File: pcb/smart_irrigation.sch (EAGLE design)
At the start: 17 parts, among them IC1 7805DT, IC2 7833DT, J1 1X2-3.5MM

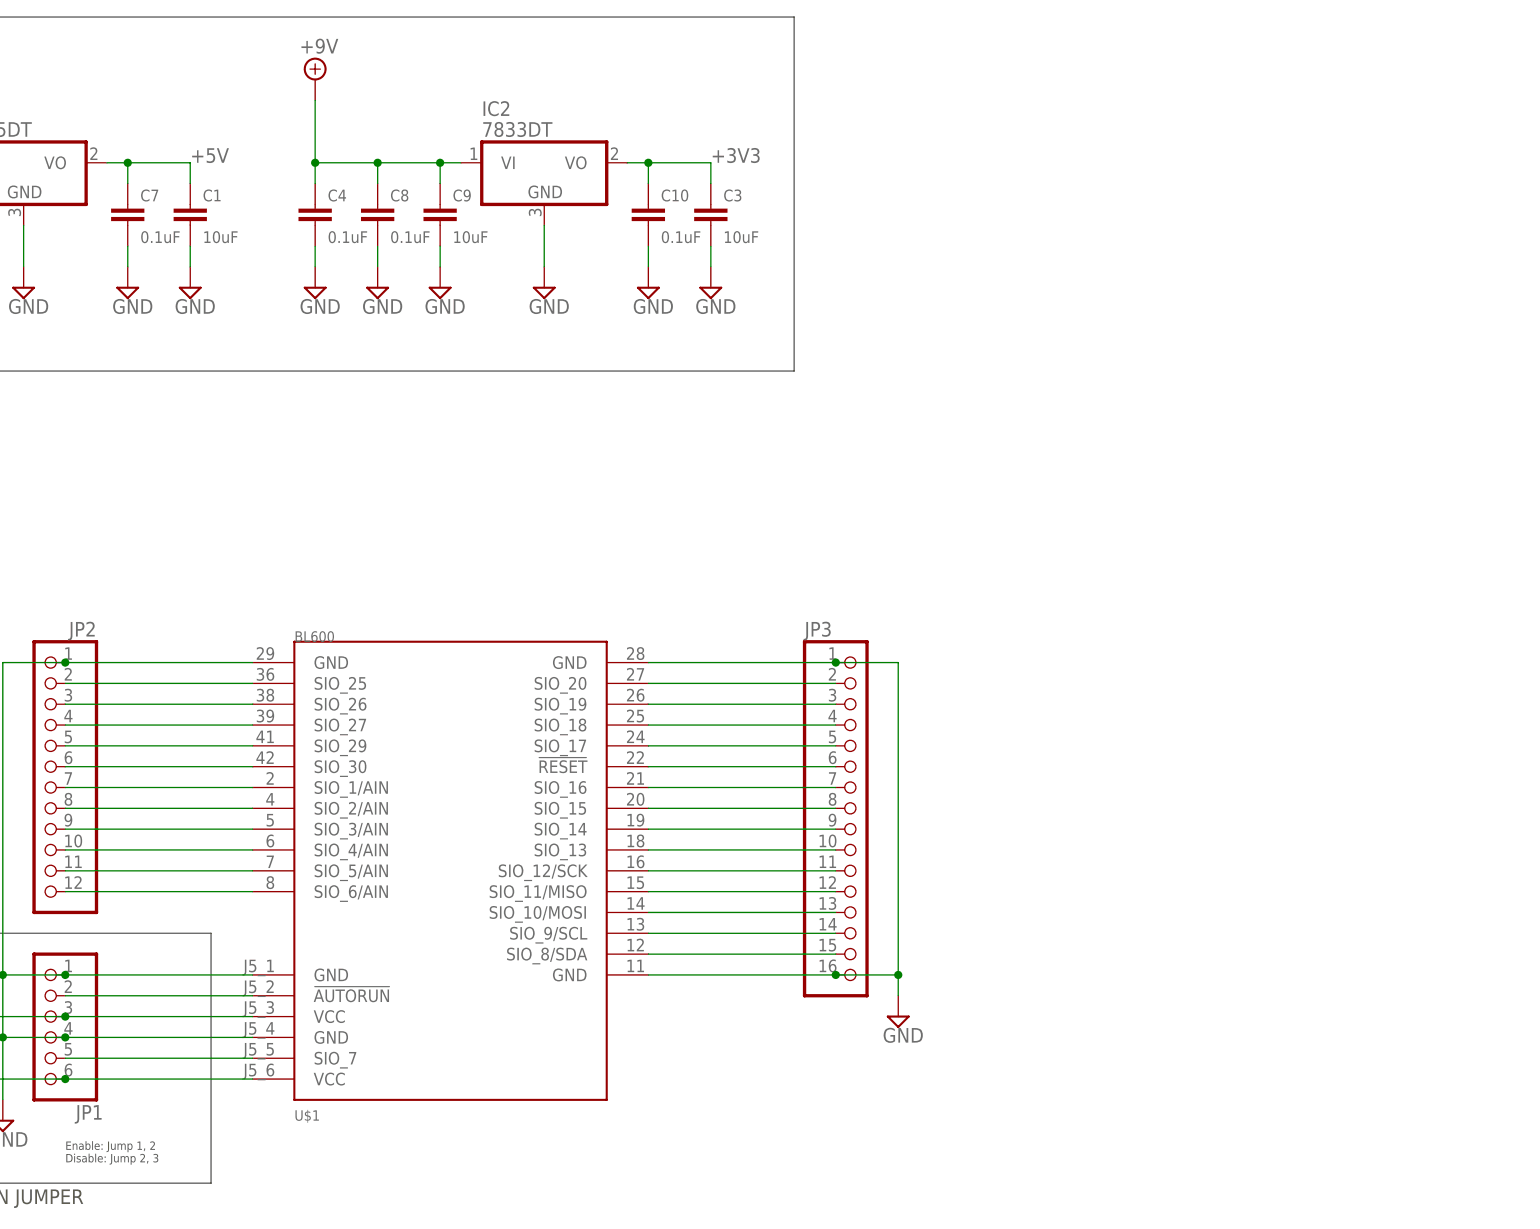
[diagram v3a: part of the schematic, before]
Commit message: PCB: Add RTC
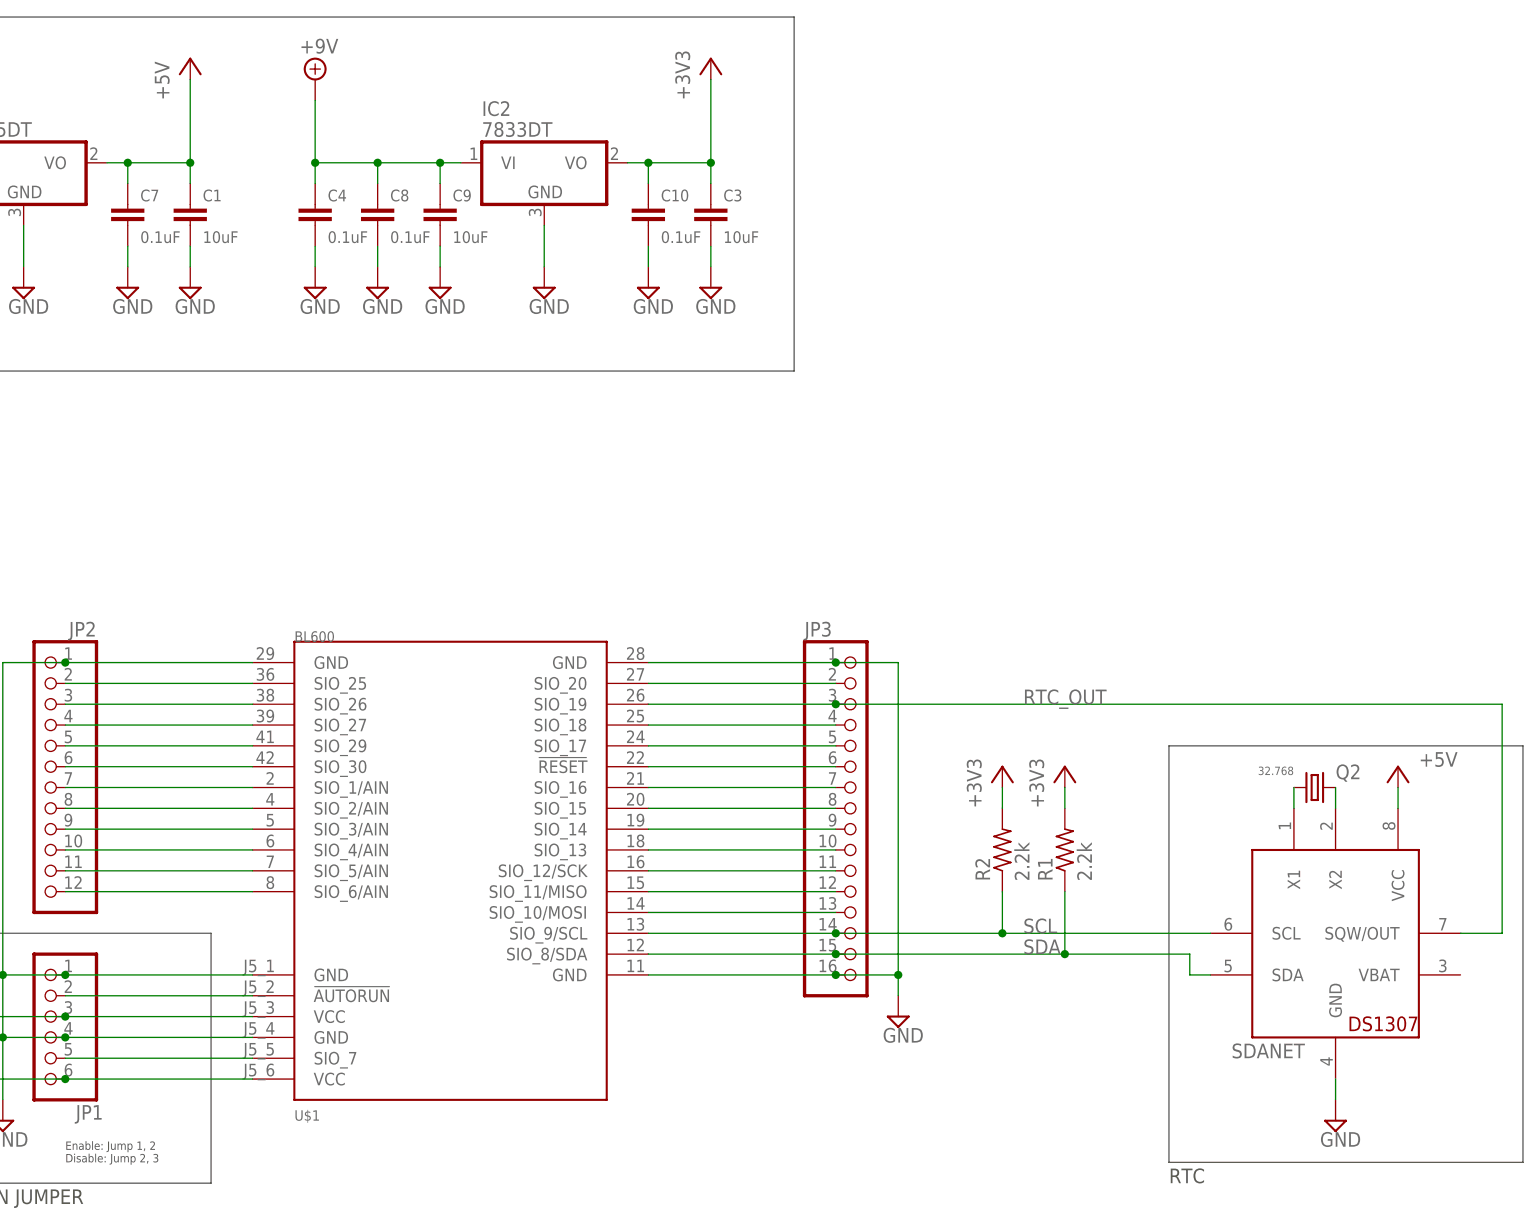
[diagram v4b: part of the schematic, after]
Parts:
- added Q2: 32.768, crystal:CRYSTALTC38H
- added R1, R2: 2.2k, rcl:R-US_M0805
- added SDANET: DS1307, adafruit:DS1307
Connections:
- removed net N$17: JP3.3, U$1.SIO_19
- removed net N$28: JP3.14, U$1.SIO_9/SCL
- removed net N$29: JP3.15, U$1.SIO_8/SDA
- new net N$15: Q2.2, SDANET.X2
- new net N$3: Q2.1, SDANET.X1
- new net RTC_OUT: JP3.3, SDANET.SQW/OUT, U$1.SIO_19
- new net SCL: JP3.14, R2.1, SDANET.SCL, U$1.SIO_9/SCL
- new net SDA: JP3.15, R1.1, SDANET.SDA, U$1.SIO_8/SDA
- net +3V3: now also R1.2, R2.2
- net +5V: now also SDANET.VCC
- net GND: now also SDANET.GND
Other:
- note added: "RTC"
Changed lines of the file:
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@@
 <part name="JP3" library="pinhead" deviceset="PINHD-1X16" device=""/>
 <part name="SUPPLY20" library="supply2" deviceset="GND" device=""/>
+<part name="SDANET" library="adafruit" deviceset="DS1307" device=""/>
+<part name="P+1" library="supply1" deviceset="+5V" device=""/>
+<part name="+3V2" library="supply1" deviceset="+3V3" device=""/>
+<part name="P+2" library="supply1" deviceset="+5V" device=""/>
+<part name="SUPPLY17" library="supply2" deviceset="GND" device=""/>
+<part name="Q2" library="crystal" deviceset="CRYSTAL" device="TC38H" value="32.768"/>
+<part name="R1" library="rcl" deviceset="R-US_" device="M0805" value="2.2k"/>
+<part name="R2" library="rcl" deviceset="R-US_" device="M0805" value="2.2k"/>
+<part name="+3V3" library="supply1" deviceset="+3V3" device=""/>
+<part name="+3V4" library="supply1" deviceset="+3V3" device=""/>
 </parts>
 <sheets>
@@
 <wire x1="58.42" y1="68.58" x2="58.42" y2="99.06" width="0.1524" layer="97"/>
 <text x="58.42" y="66.04" size="1.778" layer="97" font="vector">AUTORUN JUMPER</text>
+<wire x1="210.82" y1="71.12" x2="254" y2="71.12" width="0.1524" layer="97"/>
+<wire x1="254" y1="71.12" x2="254" y2="121.92" width="0.1524" layer="97"/>
+<wire x1="254" y1="121.92" x2="210.82" y2="121.92" width="0.1524" layer="97"/>
+<wire x1="210.82" y1="121.92" x2="210.82" y2="71.12" width="0.1524" layer="97"/>
+<text x="210.82" y="68.58" size="1.778" layer="97">RTC</text>
 </plain>
 <instances>
@@
 <instance part="JP3" gate="A" x="172.72" y="114.3"/>
 <instance part="SUPPLY20" gate="GND" x="177.8" y="88.9"/>
+<instance part="SDANET" gate="G$1" x="231.14" y="96.52"/>
+<instance part="P+1" gate="1" x="91.44" y="205.74"/>
+<instance part="+3V2" gate="G$1" x="154.94" y="205.74"/>
+<instance part="P+2" gate="1" x="238.76" y="119.38" smashed="yes">
+<attribute name="VALUE" x="241.3" y="119.38" size="1.778" layer="96"/>
+</instance>
+<instance part="SUPPLY17" gate="GND" x="231.14" y="76.2"/>
+<instance part="Q2" gate="G$1" x="228.6" y="116.84" smashed="yes">
+<attribute name="NAME" x="231.14" y="117.856" size="1.778" layer="95"/>
+<attribute name="VALUE" x="226.06" y="119.38" size="1.016" layer="96" rot="R180"/>
+</instance>
+<instance part="R1" gate="G$1" x="198.12" y="109.22" rot="R90"/>
+<instance part="R2" gate="G$1" x="190.5" y="109.22" rot="R90"/>
+<instance part="+3V3" gate="G$1" x="190.5" y="119.38"/>
+<instance part="+3V4" gate="G$1" x="198.12" y="119.38"/>
 </instances>
 <busses>
@@
 <junction x="177.8" y="93.98"/>
 </segment>
+<segment>
+<pinref part="SUPPLY17" gate="GND" pin="GND"/>
+<pinref part="SDANET" gate="G$1" pin="GND"/>
+<wire x1="231.14" y1="78.74" x2="231.14" y2="81.28" width="0.1524" layer="91"/>
+</segment>
 </net>
 <net name="+5V" class="0">
@@
 <pinref part="IC1" gate="A1" pin="VO"/>
 <wire x1="91.44" y1="193.04" x2="83.82" y2="193.04" width="0.1524" layer="91"/>
-<label x="91.44" y="193.04" size="1.778" layer="95"/>
 <pinref part="C1" gate="G$1" pin="1"/>
 <wire x1="83.82" y1="193.04" x2="81.28" y2="193.04" width="0.1524" layer="91"/>
@@
 <wire x1="83.82" y1="193.04" x2="83.82" y2="190.5" width="0.1524" layer="91"/>
 <junction x="83.82" y="193.04"/>
+<pinref part="P+1" gate="1" pin="+5V"/>
+<wire x1="91.44" y1="193.04" x2="91.44" y2="203.2" width="0.1524" layer="91"/>
+<junction x="91.44" y="193.04"/>
+</segment>
+<segment>
+<pinref part="SDANET" gate="G$1" pin="VCC"/>
+<pinref part="P+2" gate="1" pin="+5V"/>
+<wire x1="238.76" y1="116.84" x2="238.76" y2="114.3" width="0.1524" layer="91"/>
 </segment>
 </net>
@@
 <pinref part="IC2" gate="A1" pin="VO"/>
 <wire x1="154.94" y1="193.04" x2="147.32" y2="193.04" width="0.1524" layer="91"/>
-<label x="154.94" y="193.04" size="1.778" layer="95"/>
 <pinref part="C3" gate="G$1" pin="1"/>
 <wire x1="147.32" y1="193.04" x2="144.78" y2="193.04" width="0.1524" layer="91"/>
@@
 <wire x1="147.32" y1="193.04" x2="147.32" y2="190.5" width="0.1524" layer="91"/>
 <junction x="147.32" y="193.04"/>
+<pinref part="+3V2" gate="G$1" pin="+3V3"/>
+<wire x1="154.94" y1="203.2" x2="154.94" y2="193.04" width="0.1524" layer="91"/>
+<junction x="154.94" y="193.04"/>
 </segment>
 <segment>
@@
 <junction x="76.2" y="81.28"/>
 </segment>
+<segment>
+<pinref part="+3V3" gate="G$1" pin="+3V3"/>
+<pinref part="R2" gate="G$1" pin="2"/>
+<wire x1="190.5" y1="116.84" x2="190.5" y2="114.3" width="0.1524" layer="91"/>
+</segment>
+<segment>
+<pinref part="+3V4" gate="G$1" pin="+3V3"/>
+<pinref part="R1" gate="G$1" pin="2"/>
+<wire x1="198.12" y1="116.84" x2="198.12" y2="114.3" width="0.1524" layer="91"/>
+</segment>
 </net>
 <net name="N$1" class="0">
@@
 </segment>
 </net>
-<net name="N$17" class="0">
+<net name="RTC_OUT" class="0">
 <segment>
 <pinref part="U$1" gate="G$1" pin="SIO_19"/>
 <pinref part="JP3" gate="A" pin="3"/>
 <wire x1="147.32" y1="127" x2="170.18" y2="127" width="0.1524" layer="91"/>
+<pinref part="SDANET" gate="G$1" pin="SQW/OUT"/>
+<wire x1="246.38" y1="99.06" x2="251.46" y2="99.06" width="0.1524" layer="91"/>
+<wire x1="251.46" y1="99.06" x2="251.46" y2="127" width="0.1524" layer="91"/>
+<wire x1="251.46" y1="127" x2="170.18" y2="127" width="0.1524" layer="91"/>
+<junction x="170.18" y="127"/>
+<label x="193.04" y="127" size="1.778" layer="95"/>
 </segment>
 </net>
@@
 </segment>
 </net>
-<net name="N$28" class="0">
+<net name="SCL" class="0">
 <segment>
 <pinref part="JP3" gate="A" pin="14"/>
 <pinref part="U$1" gate="G$1" pin="SIO_9/SCL"/>
 <wire x1="170.18" y1="99.06" x2="147.32" y2="99.06" width="0.1524" layer="91"/>
-</segment>
-</net>
-<net name="N$29" class="0">
+<pinref part="SDANET" gate="G$1" pin="SCL"/>
+<wire x1="170.18" y1="99.06" x2="190.5" y2="99.06" width="0.1524" layer="91"/>
+<junction x="170.18" y="99.06"/>
+<label x="193.04" y="99.06" size="1.778" layer="95"/>
+<pinref part="R2" gate="G$1" pin="1"/>
+<wire x1="190.5" y1="99.06" x2="215.9" y2="99.06" width="0.1524" layer="91"/>
+<wire x1="190.5" y1="104.14" x2="190.5" y2="99.06" width="0.1524" layer="91"/>
+<junction x="190.5" y="99.06"/>
+</segment>
+</net>
+<net name="SDA" class="0">
 <segment>
 <pinref part="U$1" gate="G$1" pin="SIO_8/SDA"/>
 <pinref part="JP3" gate="A" pin="15"/>
 <wire x1="147.32" y1="96.52" x2="170.18" y2="96.52" width="0.1524" layer="91"/>
-</segment>
-</net>
+<wire x1="170.18" y1="96.52" x2="198.12" y2="96.52" width="0.1524" layer="91"/>
+<wire x1="198.12" y1="96.52" x2="213.36" y2="96.52" width="0.1524" layer="91"/>
+<wire x1="213.36" y1="96.52" x2="213.36" y2="93.98" width="0.1524" layer="91"/>
+<junction x="170.18" y="96.52"/>
+<pinref part="SDANET" gate="G$1" pin="SDA"/>
+<wire x1="213.36" y1="93.98" x2="215.9" y2="93.98" width="0.1524" layer="91"/>
+<label x="193.04" y="96.52" size="1.778" layer="95"/>
+<pinref part="R1" gate="G$1" pin="1"/>
+<wire x1="198.12" y1="104.14" x2="198.12" y2="96.52" width="0.1524" layer="91"/>
+<junction x="198.12" y="96.52"/>
+</segment>
+</net>
+<net name="N$3" class="0">
+<segment>
+<pinref part="SDANET" gate="G$1" pin="X1"/>
+<pinref part="Q2" gate="G$1" pin="1"/>
+<wire x1="226.06" y1="114.3" x2="226.06" y2="116.84" width="0.1524" layer="91"/>
+</segment>
+</net>
+<net name="N$15" class="0">
+<segment>
+<pinref part="Q2" gate="G$1" pin="2"/>
+<pinref part="SDANET" gate="G$1" pin="X2"/>
+<wire x1="231.14" y1="116.84" x2="231.14" y2="114.3" width="0.1524" layer="91"/>
+</segment>
+</net>

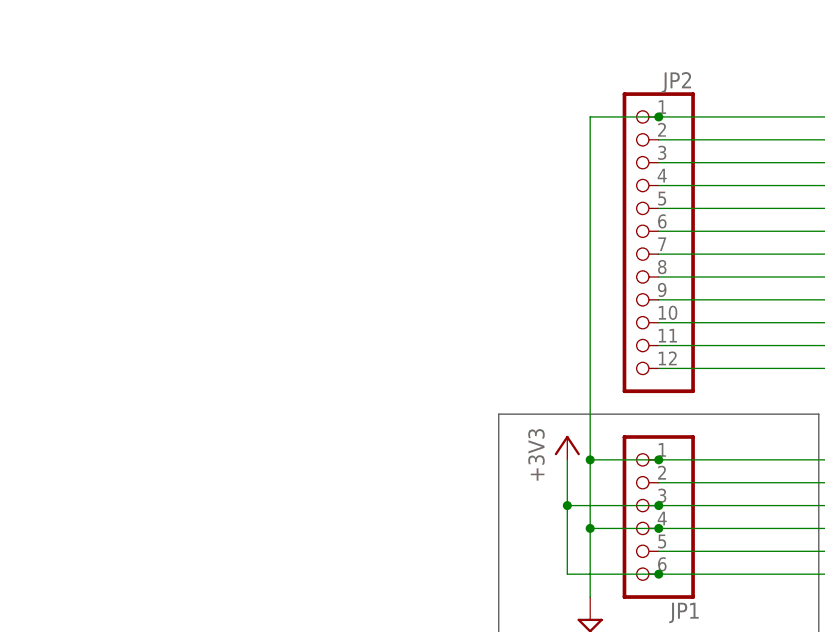
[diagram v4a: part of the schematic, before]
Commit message: PCB: Add temp sensor
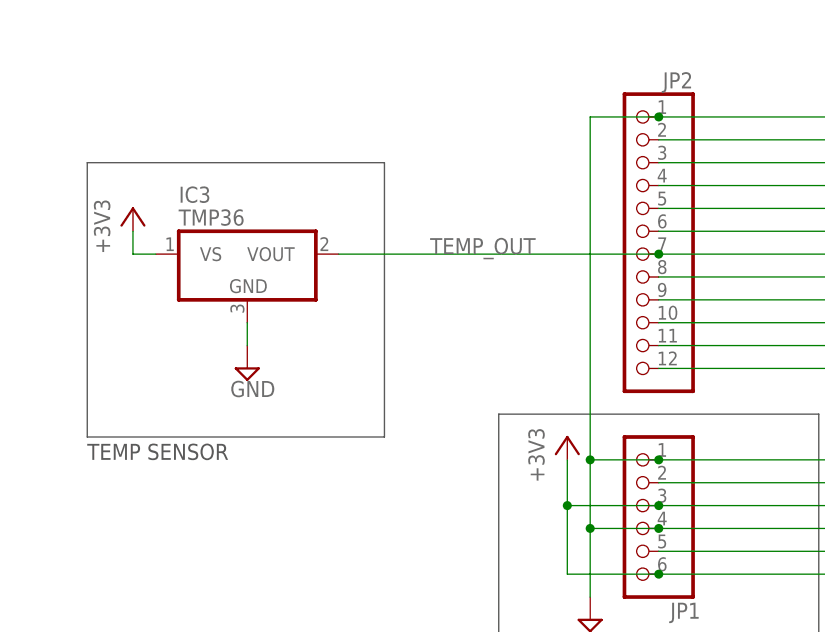
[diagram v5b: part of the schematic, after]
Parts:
- added IC3: TMP36, smart_irrigation:TMP36
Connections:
- removed net N$9: JP2.7, U$1.SIO_1/AIN
- new net TEMP_OUT: IC3.VOUT, JP2.7, U$1.SIO_1/AIN
- net +3V3: now also IC3.VS
- net GND: now also IC3.GND
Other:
- note added: "TEMP SENSOR"
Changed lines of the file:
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@@
 <part name="+3V3" library="supply1" deviceset="+3V3" device=""/>
 <part name="+3V4" library="supply1" deviceset="+3V3" device=""/>
+<part name="IC3" library="smart_irrigation" deviceset="TMP36" device=""/>
+<part name="+3V5" library="supply1" deviceset="+3V3" device=""/>
+<part name="SUPPLY18" library="supply2" deviceset="GND" device=""/>
 </parts>
 <sheets>
@@
 <wire x1="210.82" y1="121.92" x2="210.82" y2="71.12" width="0.1524" layer="97"/>
 <text x="210.82" y="68.58" size="1.778" layer="97">RTC</text>
+<wire x1="12.7" y1="127" x2="45.72" y2="127" width="0.1524" layer="97"/>
+<wire x1="45.72" y1="127" x2="45.72" y2="96.52" width="0.1524" layer="97"/>
+<wire x1="45.72" y1="96.52" x2="12.7" y2="96.52" width="0.1524" layer="97"/>
+<wire x1="12.7" y1="96.52" x2="12.7" y2="127" width="0.1524" layer="97"/>
+<text x="12.7" y="93.98" size="1.778" layer="97">TEMP SENSOR</text>
 </plain>
 <instances>
@@
 <instance part="+3V3" gate="G$1" x="190.5" y="119.38"/>
 <instance part="+3V4" gate="G$1" x="198.12" y="119.38"/>
+<instance part="IC3" gate="A1" x="30.48" y="116.84"/>
+<instance part="+3V5" gate="G$1" x="17.78" y="121.92"/>
+<instance part="SUPPLY18" gate="GND" x="30.48" y="104.14"/>
 </instances>
 <busses>
@@
 <wire x1="231.14" y1="78.74" x2="231.14" y2="81.28" width="0.1524" layer="91"/>
 </segment>
+<segment>
+<pinref part="IC3" gate="A1" pin="GND"/>
+<pinref part="SUPPLY18" gate="GND" pin="GND"/>
+<wire x1="30.48" y1="109.22" x2="30.48" y2="106.68" width="0.1524" layer="91"/>
+</segment>
 </net>
 <net name="+5V" class="0">
@@
 <wire x1="198.12" y1="116.84" x2="198.12" y2="114.3" width="0.1524" layer="91"/>
 </segment>
+<segment>
+<pinref part="+3V5" gate="G$1" pin="+3V3"/>
+<wire x1="17.78" y1="119.38" x2="17.78" y2="116.84" width="0.1524" layer="91"/>
+<pinref part="IC3" gate="A1" pin="VS"/>
+<wire x1="17.78" y1="116.84" x2="20.32" y2="116.84" width="0.1524" layer="91"/>
+</segment>
 </net>
 <net name="N$1" class="0">
@@
 </segment>
 </net>
-<net name="N$9" class="0">
+<net name="TEMP_OUT" class="0">
 <segment>
 <pinref part="JP2" gate="G$1" pin="7"/>
 <pinref part="U$1" gate="G$1" pin="SIO_1/AIN"/>
 <wire x1="76.2" y1="116.84" x2="99.06" y2="116.84" width="0.1524" layer="91"/>
-</segment>
-</net>
+<pinref part="IC3" gate="A1" pin="VOUT"/>
+<wire x1="40.64" y1="116.84" x2="76.2" y2="116.84" width="0.1524" layer="91"/>
+<junction x="76.2" y="116.84"/>
+<label x="50.8" y="116.84" size="1.778" layer="95"/>
+</segment>
+</net>
